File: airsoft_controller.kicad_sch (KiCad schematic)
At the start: 3 parts

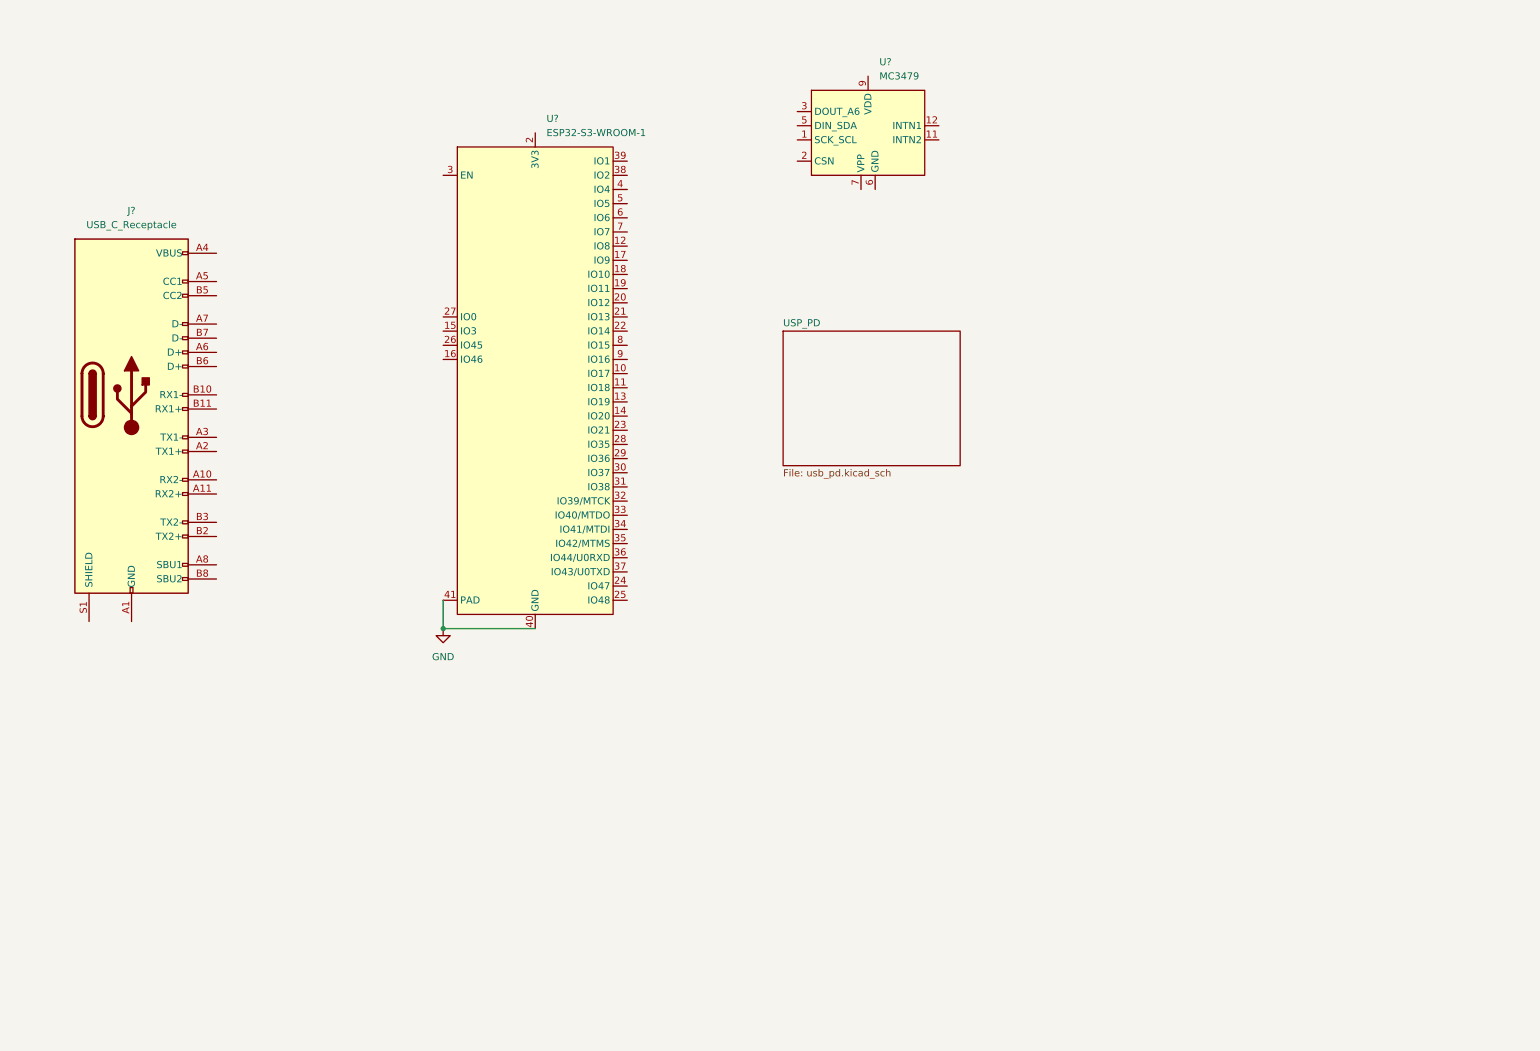
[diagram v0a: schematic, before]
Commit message: added lora, gps, nfc schematics
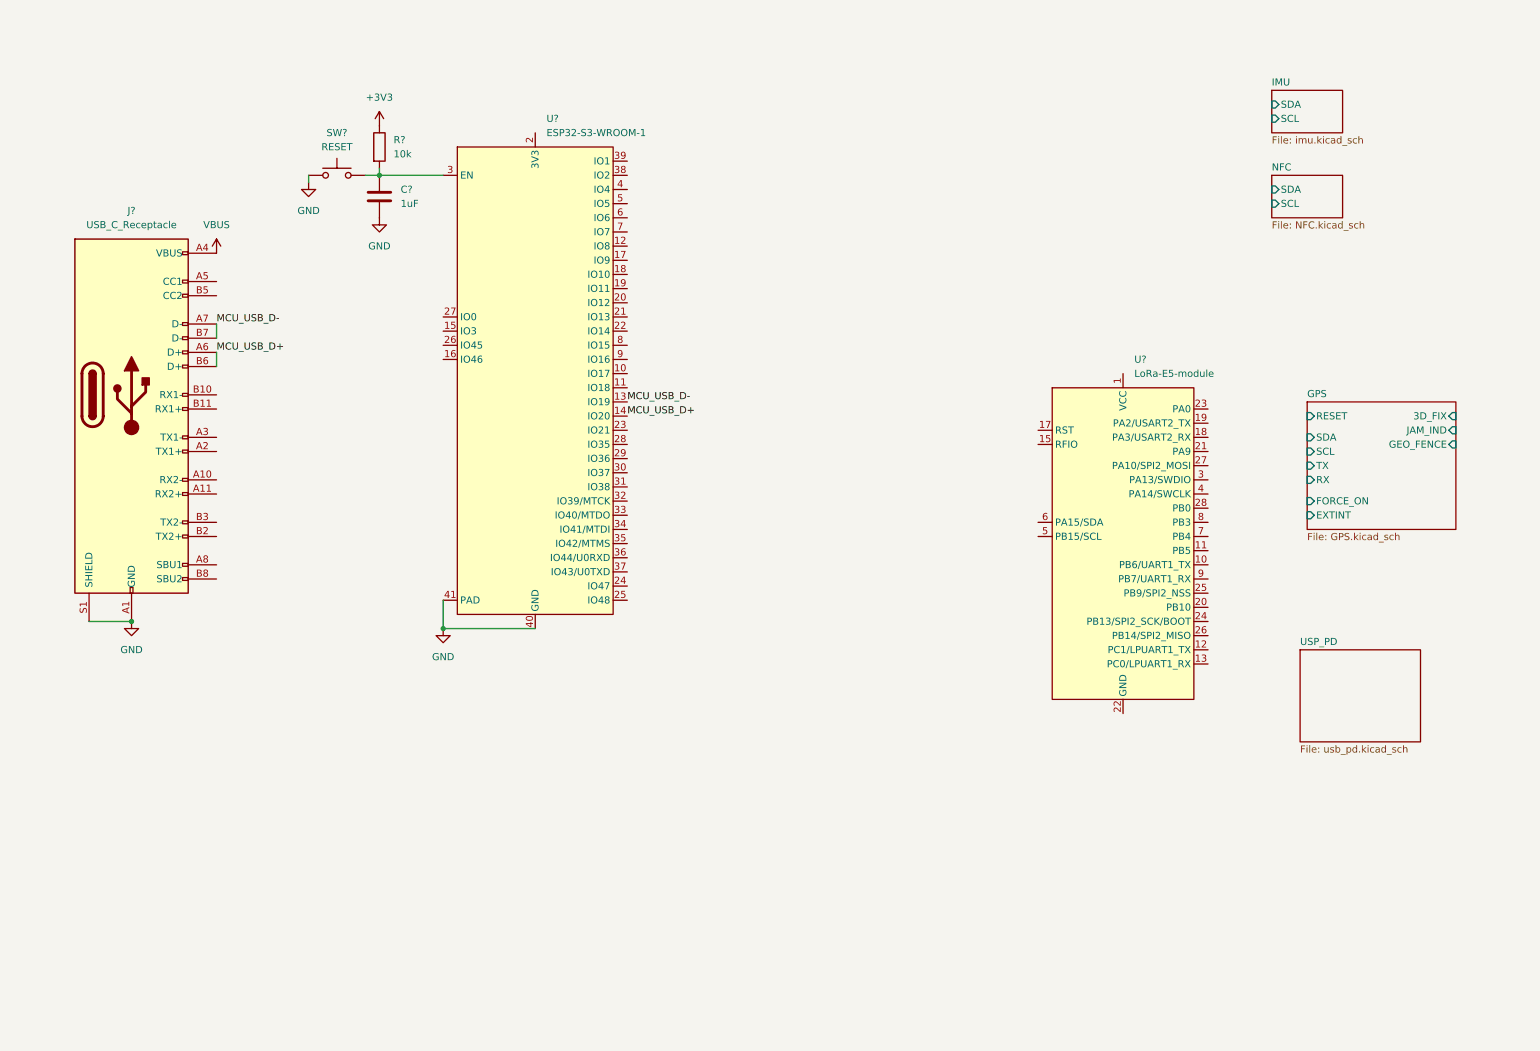
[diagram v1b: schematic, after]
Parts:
- removed U?: MC3479, Package_LGA:LGA-12_2x2mm_P0.5mm, symbol airsoft_controller:MC3479
- added C?: 1uF, symbol Device:C
- added R?: 10k, symbol Device:R
- added SW?: RESET, symbol Switch:SW_Push
- added U?: LoRa-E5-module, airsoft_controller:LoRa-E5-module, symbol airsoft_controller:LoRa-E5-module
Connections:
- net GND: now also J?.A1 (GND), J?.A12 (GND), J?.B1 (GND), J?.B12 (GND), J?.S1 (SHIELD), C?.2, SW?.1
- net VBUS: now reaches J?.A4 (VBUS), J?.A9 (VBUS), J?.B4 (VBUS), J?.B9 (VBUS)
- net MCU_USB_D+: now reaches J?.A6 (D+)
- net MCU_USB_D+: now also J?.B6 (D+), U?.14 (IO20)
- net MCU_USB_D-: now reaches J?.A7 (D-)
- net MCU_USB_D-: now also J?.B7 (D-), U?.13 (IO19)
- net at U?.3 (EN): now also C?.1, R?.2, SW?.2
- new net: U?.14 (GND), U?.16 (GND), U?.2 (GND), U?.22 (GND)
- new net +3V3: R?.1
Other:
- added sheet GPS (GPS.kicad_sch)
- added sheet IMU (imu.kicad_sch)
- added sheet NFC (NFC.kicad_sch)

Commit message: Added display, update lora sym, updated usb-pd schematic, connected sd, added external buttons
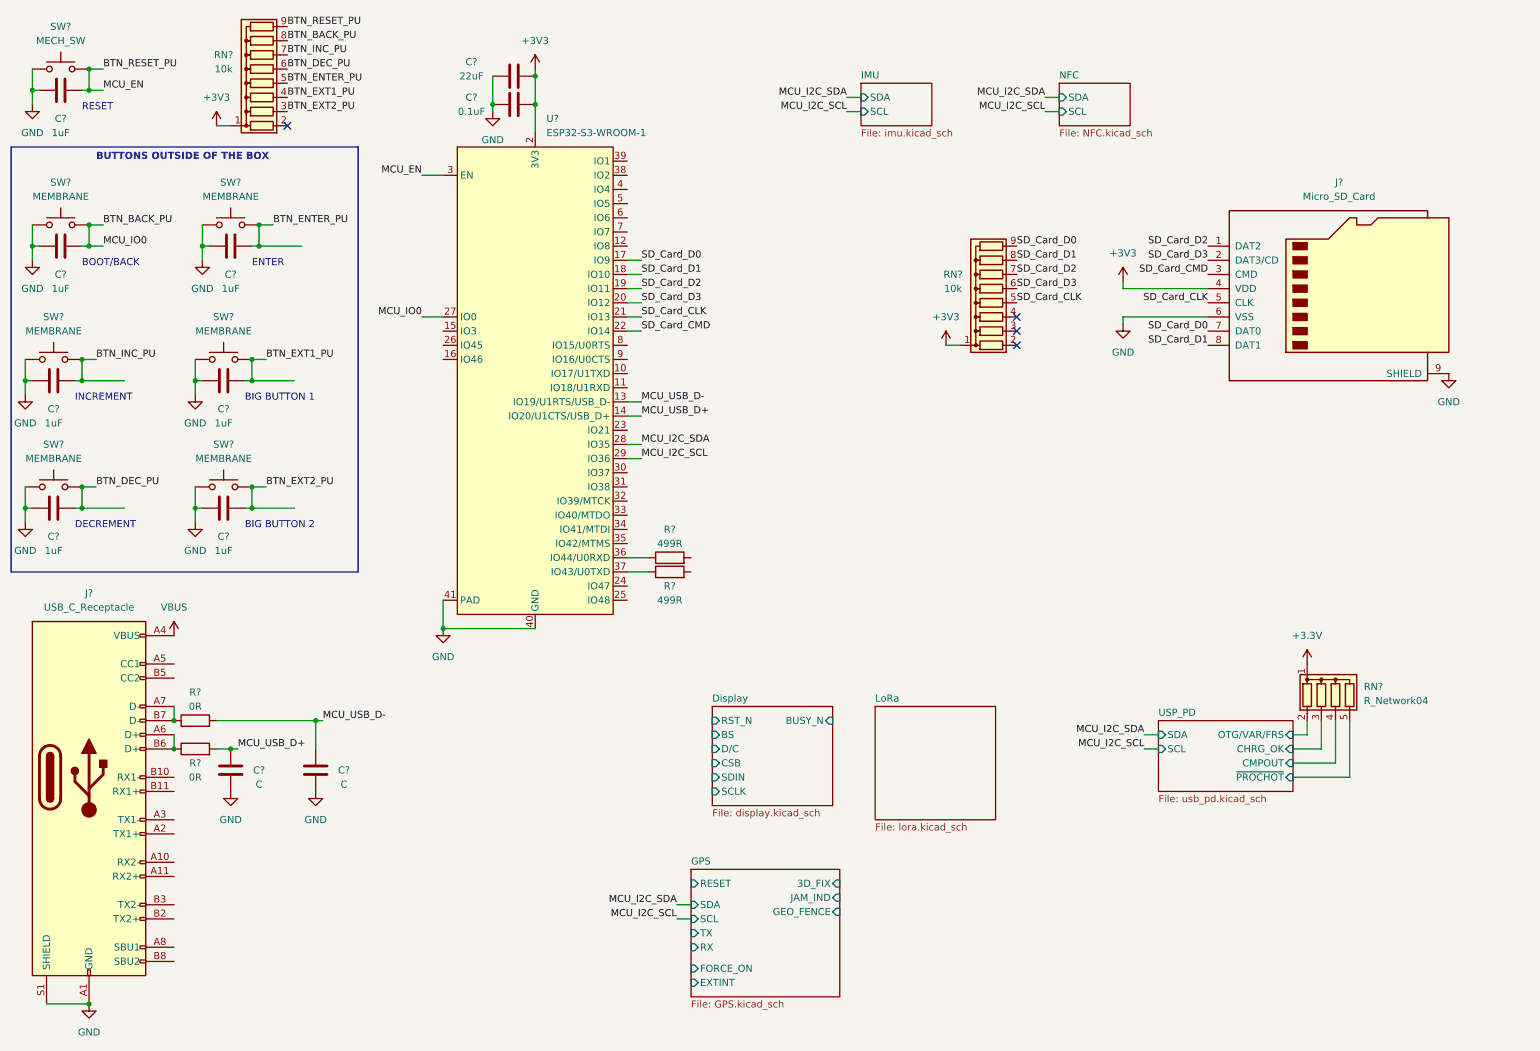
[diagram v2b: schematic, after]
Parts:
- removed C?: 1uF, symbol Device:C
- removed R?: 10k, symbol Device:R
- removed SW?: RESET, symbol Switch:SW_Push
- removed U?: LoRa-E5-module, airsoft_controller:LoRa-E5-module, symbol airsoft_controller:LoRa-E5-module
- added C? (x7): 1uF, symbol Device:C
- added C?: 22uF, symbol Device:C
- added C? (x2): C, symbol Device:C
- added C?: 0.1uF, symbol Device:C
- added J?: Micro_SD_Card, symbol Connector:Micro_SD_Card
- added R? (x2): 0R, symbol Device:R
- added R? (x2): 499R, symbol Device:R
- added RN? (x2): 10k, Resistor_THT:R_Array_SIP9, symbol Device:R_Network08
- added RN?: R_Network04, Resistor_THT:R_Array_SIP5, symbol Device:R_Network04
- added SW?: MECH_SW, symbol Switch:SW_Push
- added SW? (x6): MEMBRANE, symbol Switch:SW_Push
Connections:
- net +3V3: now also U?.2 (3V3), C?.2, C?.2, J?.4 (VDD), RN?.1 (common), RN?.1 (common)
- net GND: now also C?.1, C?.1, C?.1, C?.1, C?.2, C?.2, C?.2, C?.2, C?.2, C?.2, C?.2, J?.6 (VSS), J?.9 (SHIELD), SW?.1, SW?.1, SW?.1, SW?.1, SW?.1, SW?.1, SW?.1
- net MCU_USB_D+: now also C?.2, R?.2; no longer J?.A6 (D+), J?.B6 (D+)
- net MCU_USB_D-: now also C?.2, R?.2; no longer J?.A7 (D-), J?.B7 (D-)
- net BTN_RESET_PU: now reaches U?.3 (EN)
- net BTN_RESET_PU: now also C?.1, RN?.9 (R8), SW?.2
- net SD_Card_D0: now reaches U?.17 (IO9)
- net SD_Card_D0: now also J?.7 (DAT0), RN?.9 (R8)
- net SD_Card_D1: now reaches U?.18 (IO10)
- net SD_Card_D1: now also J?.8 (DAT1), RN?.8 (R7)
- net SD_Card_D2: now reaches U?.19 (IO11)
- net SD_Card_D2: now also J?.1 (DAT2), RN?.7 (R6)
- net SD_Card_D3: now reaches U?.20 (IO12)
- net SD_Card_D3: now also J?.2 (DAT3/CD), RN?.6 (R5)
- net SD_Card_CLK: now reaches U?.21 (IO13)
- net SD_Card_CLK: now also J?.5 (CLK), RN?.5 (R4)
- net SD_Card_CMD: now reaches U?.22 (IO14)
- net SD_Card_CMD: now also J?.3 (CMD)
- net BTN_BACK_PU: now reaches U?.27 (IO0)
- net BTN_BACK_PU: now also C?.1, RN?.8 (R7), SW?.2
- net MCU_I2C_SDA: now reaches U?.28 (IO35)
- net MCU_I2C_SCL: now reaches U?.29 (IO36)
- net at U?.36 (IO44/U0RXD): now also R?.1
- net at U?.37 (IO43/U0TXD): now also R?.1
- new net: J?.A6 (D+), J?.B6 (D+), R?.1
- new net: J?.A7 (D-), J?.B7 (D-), R?.1
- new net +3.3V: RN?.1 (common)
- new net BTN_DEC_PU: C?.1, RN?.6 (R5), SW?.2
- new net BTN_ENTER_PU: C?.1, RN?.5 (R4), SW?.2
- new net BTN_EXT1_PU: C?.1, RN?.4 (R3), SW?.2
- new net BTN_EXT2_PU: C?.1, RN?.3 (R2), SW?.2
- new net BTN_INC_PU: C?.1, RN?.7 (R6), SW?.2
- new net USP_PD/CHRG_OK: RN?.3 (R2)
- new net USP_PD/CMPOUT: RN?.4 (R3)
- new net USP_PD/OTG/VAR/FRS: RN?.2 (R1)
- new net USP_PD/~{PROCHOT}: RN?.5 (R4)
- no-connect marks 0 -> 4
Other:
- added sheet Display (display.kicad_sch)
- added sheet LoRa (lora.kicad_sch)
- sheet USP_PD ports: added CHRG_OK, CMPOUT, OTG/VAR/FRS, SCL, SDA, ~{PROCHOT}; removed none
- note added: "BIG BUTTON 1"
- note added: "BIG BUTTON 2"
- note added: "BOOT/BACK"
- note added: "BUTTONS OUTSIDE OF THE BOX"
- note added: "DECREMENT"
- note added: "ENTER"
- note added: "INCREMENT"
- note added: "RESET"
- moved on the sheet: J?

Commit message: Added new lora, added rgb leds, updated TSP65988 schematic, added bat to 3v3, added battery balancer
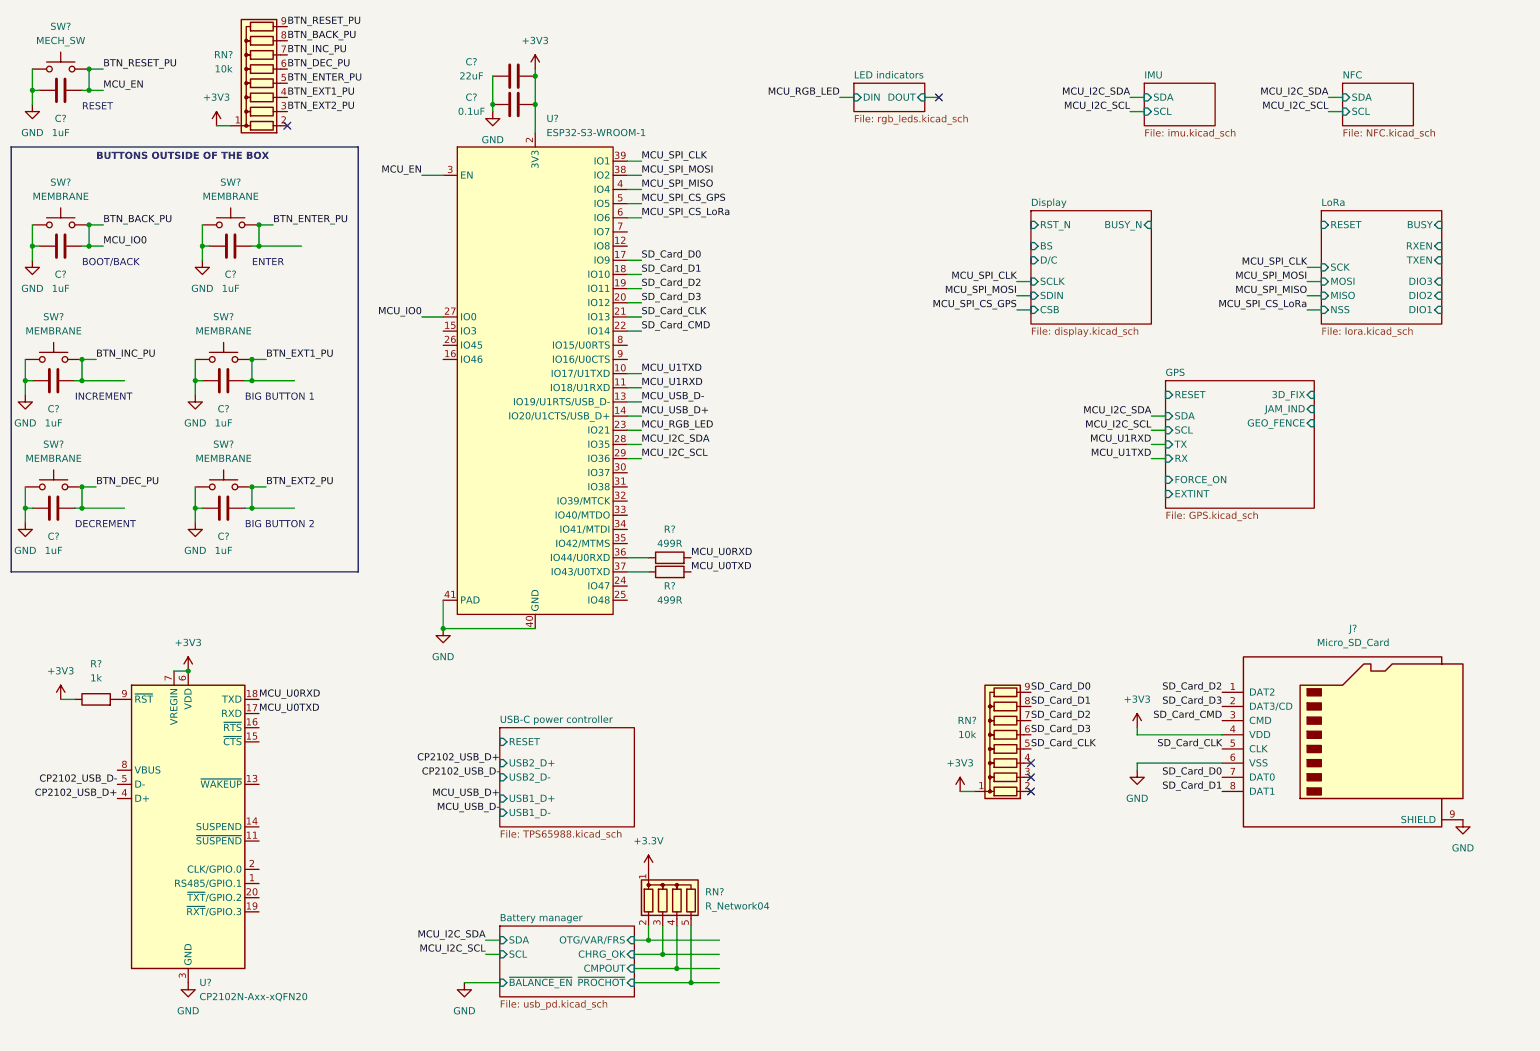
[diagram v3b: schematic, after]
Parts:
- removed C? (x2): C, symbol Device:C
- removed J?: USB_C_Receptacle, symbol Connector:USB_C_Receptacle
- removed R? (x2): 0R, symbol Device:R
- removed RN?: R_Network04, Resistor_THT:R_Array_SIP5, symbol Device:R_Network04
- added R?: 1k, symbol Device:R
- added RN?: R_Network04, Resistor_THT:R_Array_SIP5, symbol Device:R_Network04
- added U?: CP2102N-Axx-xQFN20, Package_DFN_QFN:SiliconLabs_QFN-20-1EP_3x3mm_P0.5mm, symbol Interface_USB:CP2102N-Axx-xQFN20
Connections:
- net +3.3V: now also RN?.1 (common)
- net +3V3: now also R?.1, U?.6 (VDD), U?.7 (VREGIN)
- net GND: now also U?.12 (GND), U?.21 (GND), U?.3 (GND)
- net MCU_U0TXD: now reaches R?.2
- net MCU_U0TXD: now also U?.17 (RXD)
- net MCU_U0RXD: now reaches R?.2
- net MCU_U0RXD: now also U?.18 (TXD)
- net MCU_U1TXD: now reaches U?.10 (IO17/U1TXD)
- net MCU_U1RXD: now reaches U?.11 (IO18/U1RXD)
- net MCU_RGB_LED: now reaches U?.23 (IO21)
- net MCU_SPI_MOSI: now reaches U?.38 (IO2)
- net MCU_SPI_CLK: now reaches U?.39 (IO1)
- net MCU_SPI_MISO: now reaches U?.4 (IO4)
- net MCU_SPI_CS_GPS: now reaches U?.5 (IO5)
- net MCU_SPI_CS_LoRa: now reaches U?.6 (IO6)
- new net: R?.2, U?.9 (~{RST})
- new net Battery manager/CHRG_OK: RN?.3 (R2)
- new net Battery manager/CMPOUT: RN?.4 (R3)
- new net Battery manager/OTG/VAR/FRS: RN?.2 (R1)
- new net Battery manager/~{PROCHOT}: RN?.5 (R4)
- new net CP2102_USB_D+: U?.4 (D+)
- new net CP2102_USB_D-: U?.5 (D-)
- no-connect marks 4 -> 5
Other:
- removed sheet USP_PD
- added sheet Battery manager (usb_pd.kicad_sch)
- added sheet LED indicators (rgb_leds.kicad_sch)
- added sheet USB-C power controller (TPS65988.kicad_sch)
- sheet LoRa ports: added BUSY, DIO1, DIO2, DIO3, MISO, MOSI, NSS, RESET, RXEN, SCK, TXEN; removed none
- moved on the sheet: J?, RN?

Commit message: added digi-pote symbol, added USB_source voltage regulators
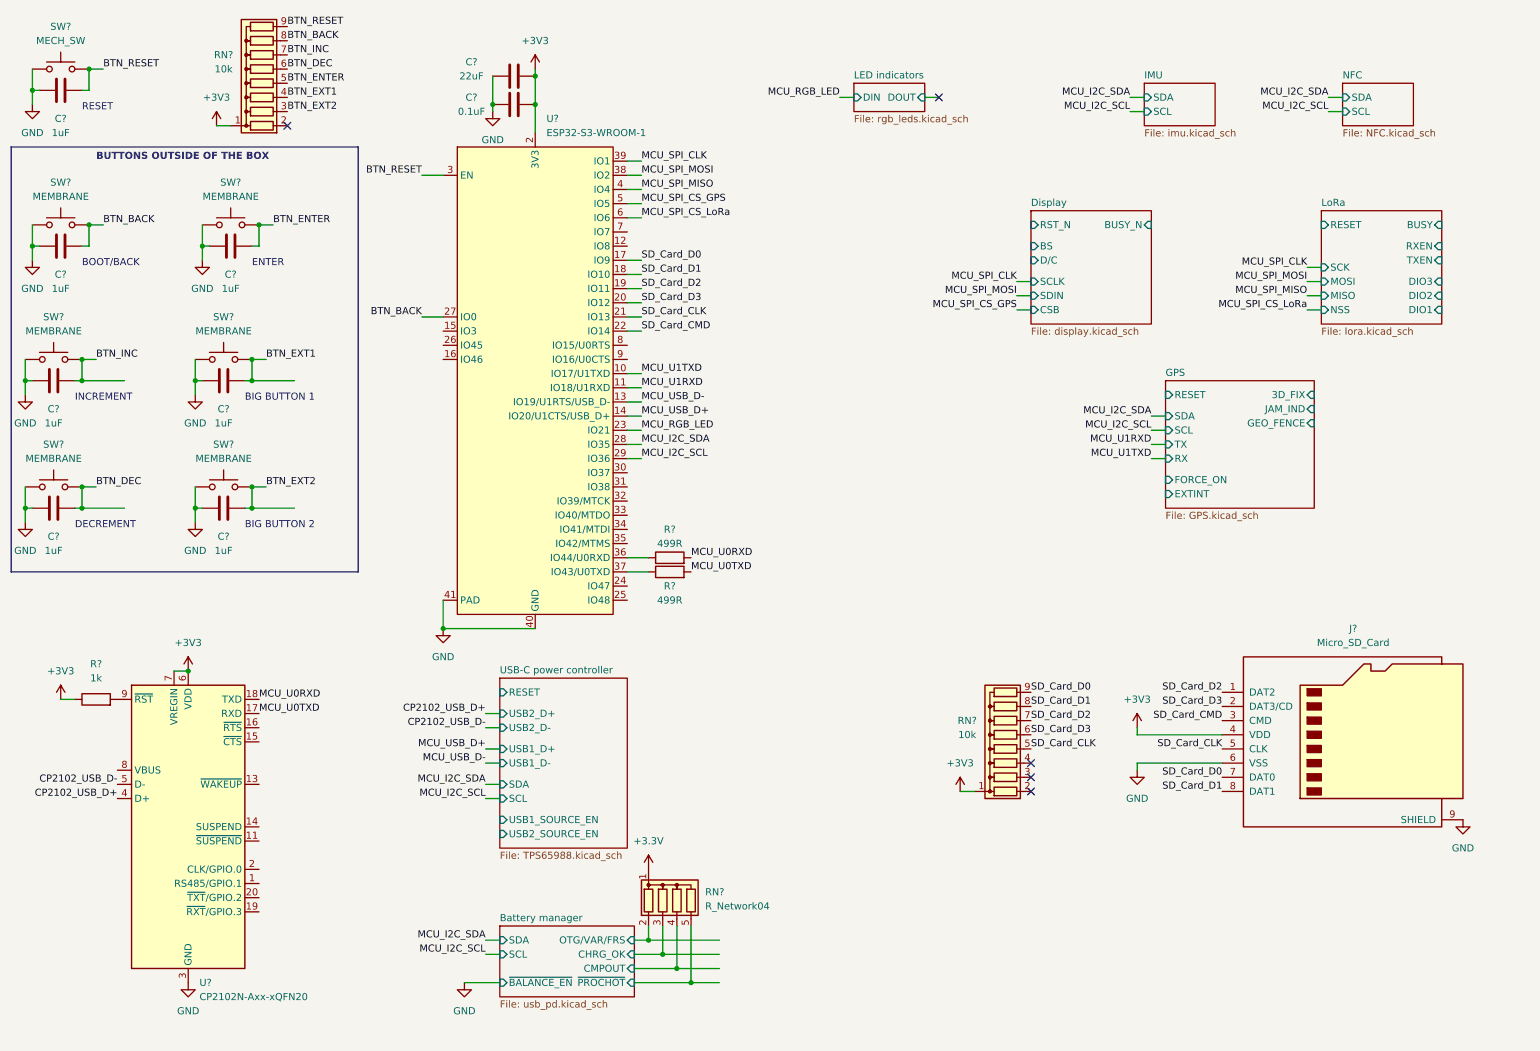
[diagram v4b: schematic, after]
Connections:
- net BTN_BACK_PU renamed BTN_BACK
- net BTN_DEC_PU renamed BTN_DEC
- net BTN_ENTER_PU renamed BTN_ENTER
- net BTN_EXT1_PU renamed BTN_EXT1
- net BTN_EXT2_PU renamed BTN_EXT2
- net BTN_INC_PU renamed BTN_INC
- net BTN_RESET_PU renamed BTN_RESET
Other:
- sheet USB-C power controller ports: added SCL, SDA, USB1_SOURCE_EN, USB2_SOURCE_EN; removed none
